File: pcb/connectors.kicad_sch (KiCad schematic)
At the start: 7 parts, among them J1 USB_C_Receptacle_USB2.0, J5 Conn_01x04, U6 USBLC6-2SC6

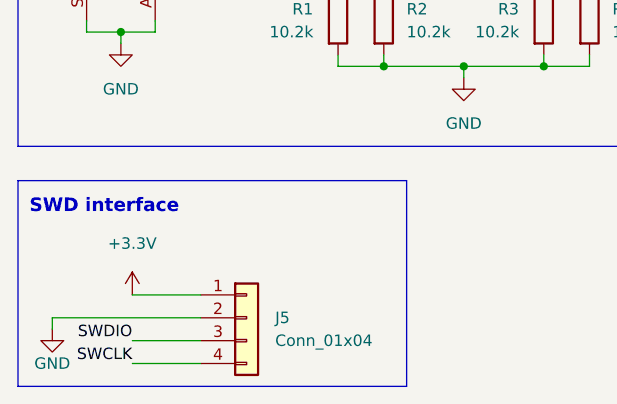
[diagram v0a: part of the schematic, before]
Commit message: Finished off schematic
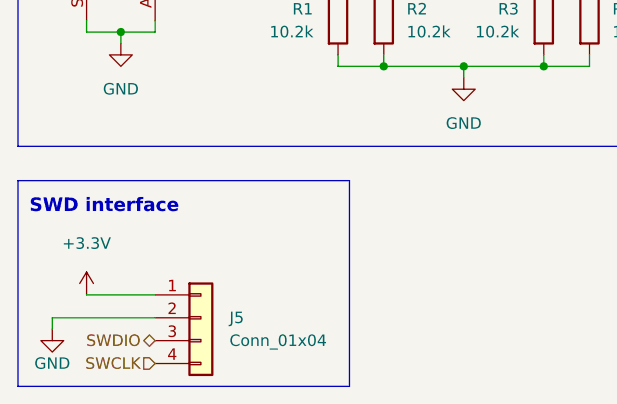
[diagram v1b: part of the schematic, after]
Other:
- moved on the sheet: J5
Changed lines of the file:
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@@
-    (stroke (width 0) (type default))
-  )
-  (wire (pts (xy 38.1 115.57) (xy 45.72 115.57))
     (stroke (width 0) (type default))
   )
@@
     (stroke (width 0) (type default))
   )
-  (wire (pts (xy 38.1 113.03) (xy 45.72 113.03))
-    (stroke (width 0) (type default))
-  )
-  (polyline (pts (xy 68.58 118.11) (xy 25.4 118.11))
+  (polyline (pts (xy 62.23 118.11) (xy 25.4 118.11))
     (stroke (width 0) (type default))
   )
@@
     (stroke (width 0) (type default))
   )
-  (wire (pts (xy 38.1 107.95) (xy 45.72 107.95))
+  (wire (pts (xy 33.02 107.95) (xy 40.64 107.95))
     (stroke (width 0) (type default))
   )
@@
     (stroke (width 0) (type default))
   )
-  (polyline (pts (xy 68.58 95.25) (xy 68.58 118.11))
+  (polyline (pts (xy 62.23 95.25) (xy 62.23 118.11))
     (stroke (width 0) (type default))
   )
@@
     (stroke (width 0) (type default))
   )
-  (wire (pts (xy 29.21 110.49) (xy 45.72 110.49))
+  (wire (pts (xy 29.21 110.49) (xy 40.64 110.49))
     (stroke (width 0) (type default))
   )
@@
     (stroke (width 0) (type default))
   )
-  (polyline (pts (xy 25.4 95.25) (xy 68.58 95.25))
+  (polyline (pts (xy 25.4 95.25) (xy 62.23 95.25))
     (stroke (width 0) (type default))
   )
@@
     (effects (font (size 1.27 1.27)) (justify right bottom))
   )
-  (label "SWDIO" (at 38.1 113.03 180) (fields_autoplaced)
-    (effects (font (size 1.27 1.27)) (justify right bottom))
-  )
-  (label "SWCLK" (at 38.1 115.57 180) (fields_autoplaced)
-    (effects (font (size 1.27 1.27)) (justify right bottom))
-  )
   (hierarchical_label "USB_D+" (shape bidirectional) (at 80.01 66.04 0) (fields_autoplaced)
     (effects (font (size 1.27 1.27)) (justify left))
+  )
+  (hierarchical_label "SWCLK" (shape input) (at 40.64 115.57 180) (fields_autoplaced)
+    (effects (font (size 1.27 1.27)) (justify right))
+  )
+  (hierarchical_label "SWDIO" (shape bidirectional) (at 40.64 113.03 180) (fields_autoplaced)
+    (effects (font (size 1.27 1.27)) (justify right))
   )
   (hierarchical_label "USB_D-" (shape bidirectional) (at 80.01 45.72 0) (fields_autoplaced)
@@
     )
   )
-  (symbol (lib_id "power:+3.3V") (at 38.1 107.95 0) (unit 1)
-    (in_bom yes) (on_board yes) (dnp no) (fields_autoplaced)
-    (property "Reference" "#PWR041" (at 38.1 111.76 0)
-      (effects (font (size 1.27 1.27)) hide)
-    )
-    (property "Value" "+3.3V" (at 38.1 102.235 0)
-      (effects (font (size 1.27 1.27)))
-    )
-    (property "Footprint" "" (at 38.1 107.95 0)
-      (effects (font (size 1.27 1.27)) hide)
-    )
-    (property "Datasheet" "" (at 38.1 107.95 0)
+  (symbol (lib_id "power:+3.3V") (at 33.02 107.95 0) (unit 1)
+    (in_bom yes) (on_board yes) (dnp no) (fields_autoplaced)
+    (property "Reference" "#PWR041" (at 33.02 111.76 0)
+      (effects (font (size 1.27 1.27)) hide)
+    )
+    (property "Value" "+3.3V" (at 33.02 102.235 0)
+      (effects (font (size 1.27 1.27)))
+    )
+    (property "Footprint" "" (at 33.02 107.95 0)
+      (effects (font (size 1.27 1.27)) hide)
+    )
+    (property "Datasheet" "" (at 33.02 107.95 0)
       (effects (font (size 1.27 1.27)) hide)
     )
@@
       (project "keyboard"
         (path "/fc529d87-72d0-4c92-b352-ddcf4c6f7199/953c467c-8c0d-4158-80e9-7f51ef1515ee"
-          (reference "#PWR012") (unit 1)
+          (reference "#PWR011") (unit 1)
         )
       )
@@
     )
   )
-  (symbol (lib_id "Connector_Generic:Conn_01x04") (at 50.8 110.49 0) (unit 1)
-    (in_bom yes) (on_board yes) (dnp no) (fields_autoplaced)
-    (property "Reference" "J5" (at 53.975 110.4899 0)
+  (symbol (lib_id "Connector_Generic:Conn_01x04") (at 45.72 110.49 0) (unit 1)
+    (in_bom yes) (on_board yes) (dnp no) (fields_autoplaced)
+    (property "Reference" "J5" (at 48.895 110.4899 0)
       (effects (font (size 1.27 1.27)) (justify left))
     )
-    (property "Value" "Conn_01x04" (at 53.975 113.0299 0)
+    (property "Value" "Conn_01x04" (at 48.895 113.0299 0)
       (effects (font (size 1.27 1.27)) (justify left))
     )
-    (property "Footprint" "Connector_PinHeader_2.54mm:PinHeader_1x04_P2.54mm_Vertical" (at 50.8 110.49 0)
-      (effects (font (size 1.27 1.27)) hide)
-    )
-    (property "Datasheet" "~" (at 50.8 110.49 0)
+    (property "Footprint" "Connector_PinHeader_2.54mm:PinHeader_1x04_P2.54mm_Vertical" (at 45.72 110.49 0)
+      (effects (font (size 1.27 1.27)) hide)
+    )
+    (property "Datasheet" "~" (at 45.72 110.49 0)
       (effects (font (size 1.27 1.27)) hide)
     )
@@
   (symbol (lib_id "power:GND") (at 36.83 80.01 0) (unit 1)
     (in_bom yes) (on_board yes) (dnp no) (fields_autoplaced)
-    (property "Reference" "#PWR011" (at 36.83 86.36 0)
+    (property "Reference" "#PWR012" (at 36.83 86.36 0)
       (effects (font (size 1.27 1.27)) hide)
     )
@@
       (project "keyboard"
         (path "/fc529d87-72d0-4c92-b352-ddcf4c6f7199/953c467c-8c0d-4158-80e9-7f51ef1515ee"
-          (reference "#PWR011") (unit 1)
-        )
-      )
+          (reference "#PWR012") (unit 1)
+        )
+      )

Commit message: Started routing
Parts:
- J5: footprint Connector_PinHeader_2.54mm:PinHeader_1x04_P2.54mm_Vertical -> Connector_PinSocket_2.54mm:PinSocket_1x04_P2.54mm_Vertical
- R1, R2, R3, R4: footprint Resistor_SMD:R_0201_0603Metric -> Resistor_SMD:R_0603_1608Metric
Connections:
- net VBUS: now reaches J1.A4 (VBUS), J1.A9 (VBUS), J1.B4 (VBUS), J1.B9 (VBUS), U6.5 (VBUS)
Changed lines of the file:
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@@
   (junction (at 57.15 53.34) (diameter 0) (color 0 0 0 0)
+  )
+  (junction (at 73.66 39.37) (diameter 0) (color 0 0 0 0)
   )
   (junction (at 86.36 72.39) (diameter 0) (color 0 0 0 0)
@@
     (stroke (width 0) (type default))
   )
+  (wire (pts (xy 73.66 39.37) (xy 90.17 39.37))
+    (stroke (width 0) (type default))
+  )
   (wire (pts (xy 78.74 45.72) (xy 80.01 45.72))
     (stroke (width 0) (type default))
@@
     (stroke (width 0) (type default))
   )
+  (wire (pts (xy 73.66 38.1) (xy 73.66 39.37))
+    (stroke (width 0) (type default))
+  )
   (wire (pts (xy 90.17 55.88) (xy 86.36 55.88))
     (stroke (width 0) (type default))
   )
-  (wire (pts (xy 55.88 39.37) (xy 90.17 39.37))
+  (wire (pts (xy 55.88 39.37) (xy 73.66 39.37))
     (stroke (width 0) (type default))
   )
@@
         (path "/fc529d87-72d0-4c92-b352-ddcf4c6f7199/953c467c-8c0d-4158-80e9-7f51ef1515ee"
           (reference "U2") (unit 1)
+        )
+      )
+    )
+  )
+  (symbol (lib_id "Device:R") (at 88.9 77.47 0) (unit 1)
+    (in_bom yes) (on_board yes) (dnp no)
+    (property "Reference" "R4" (at 91.44 76.2 0)
+      (effects (font (size 1.27 1.27)) (justify left))
+    )
+    (property "Value" "10.2k" (at 91.44 78.74 0)
+      (effects (font (size 1.27 1.27)) (justify left))
+    )
+    (property "Footprint" "Resistor_SMD:R_0603_1608Metric" (at 87.122 77.47 90)
+      (effects (font (size 1.27 1.27)) hide)
+    )
+    (property "Datasheet" "~" (at 88.9 77.47 0)
+      (effects (font (size 1.27 1.27)) hide)
+    )
+    (pin "1")
+    (pin "2")
+    (instances
+      (project "keyboard"
+        (path "/fc529d87-72d0-4c92-b352-ddcf4c6f7199/953c467c-8c0d-4158-80e9-7f51ef1515ee"
+          (reference "R4") (unit 1)
         )
       )
@@
       (effects (font (size 1.27 1.27)) (justify left))
     )
-    (property "Footprint" "Connector_PinHeader_2.54mm:PinHeader_1x04_P2.54mm_Vertical" (at 45.72 110.49 0)
+    (property "Footprint" "Connector_PinSocket_2.54mm:PinSocket_1x04_P2.54mm_Vertical" (at 45.72 110.49 0)
       (effects (font (size 1.27 1.27)) hide)
     )
@@
     )
   )
+  (symbol (lib_id "power:VBUS") (at 73.66 38.1 0) (unit 1)
+    (in_bom yes) (on_board yes) (dnp no) (fields_autoplaced)
+    (property "Reference" "#PWR034" (at 73.66 41.91 0)
+      (effects (font (size 1.27 1.27)) hide)
+    )
+    (property "Value" "VBUS" (at 73.66 34.29 0)
+      (effects (font (size 1.27 1.27)))
+    )
+    (property "Footprint" "" (at 73.66 38.1 0)
+      (effects (font (size 1.27 1.27)) hide)
+    )
+    (property "Datasheet" "" (at 73.66 38.1 0)
+      (effects (font (size 1.27 1.27)) hide)
+    )
+    (pin "1")
+    (instances
+      (project "keyboard"
+        (path "/fc529d87-72d0-4c92-b352-ddcf4c6f7199/953c467c-8c0d-4158-80e9-7f51ef1515ee"
+          (reference "#PWR034") (unit 1)
+        )
+      )
+    )
+  )
   (symbol (lib_id "Device:R") (at 83.82 77.47 0) (unit 1)
     (in_bom yes) (on_board yes) (dnp no)
@@
       (effects (font (size 1.27 1.27)) (justify left))
     )
-    (property "Footprint" "Resistor_SMD:R_0201_0603Metric" (at 82.042 77.47 90)
+    (property "Footprint" "Resistor_SMD:R_0603_1608Metric" (at 82.042 77.47 90)
       (effects (font (size 1.27 1.27)) hide)
     )
@@
         (path "/fc529d87-72d0-4c92-b352-ddcf4c6f7199/953c467c-8c0d-4158-80e9-7f51ef1515ee"
           (reference "R3") (unit 1)
-        )
-      )
-    )
-  )
-  (symbol (lib_id "Device:R") (at 88.9 77.47 0) (unit 1)
-    (in_bom yes) (on_board yes) (dnp no)
-    (property "Reference" "R4" (at 91.44 76.2 0)
-      (effects (font (size 1.27 1.27)) (justify left))
-    )
-    (property "Value" "10.2k" (at 91.44 78.74 0)
-      (effects (font (size 1.27 1.27)) (justify left))
-    )
-    (property "Footprint" "Resistor_SMD:R_0201_0603Metric" (at 87.122 77.47 90)
-      (effects (font (size 1.27 1.27)) hide)
-    )
-    (property "Datasheet" "~" (at 88.9 77.47 0)
-      (effects (font (size 1.27 1.27)) hide)
-    )
-    (pin "1")
-    (pin "2")
-    (instances
-      (project "keyboard"
-        (path "/fc529d87-72d0-4c92-b352-ddcf4c6f7199/953c467c-8c0d-4158-80e9-7f51ef1515ee"
-          (reference "R4") (unit 1)
         )
       )
@@
       (effects (font (size 1.27 1.27)) (justify left))
     )
-    (property "Footprint" "Resistor_SMD:R_0201_0603Metric" (at 59.182 77.47 90)
+    (property "Footprint" "Resistor_SMD:R_0603_1608Metric" (at 59.182 77.47 90)
       (effects (font (size 1.27 1.27)) hide)
     )
@@
       (effects (font (size 1.27 1.27)) (justify left))
     )
-    (property "Footprint" "Resistor_SMD:R_0201_0603Metric" (at 64.262 77.47 90)
-      (effects (font (size 1.27 1.27)) hide)
-    )
+    (property "Footprint" "Resistor_SMD:R_0603_1608Metric" (at 64.262 77.47 90)
+      (effects (font (size 1.27 1.27)) hide)
+    )

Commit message: Finished routing, ready for checks
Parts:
- J5: footprint Connector_PinSocket_2.54mm:PinSocket_1x04_P2.54mm_Vertical -> Connector_PinSocket_2.54mm:PinSocket_1x04_P2.54mm_Horizontal
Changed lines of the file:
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@@
       (effects (font (size 1.27 1.27)) (justify left))
     )
-    (property "Footprint" "Connector_PinSocket_2.54mm:PinSocket_1x04_P2.54mm_Vertical" (at 45.72 110.49 0)
+    (property "Footprint" "Connector_PinSocket_2.54mm:PinSocket_1x04_P2.54mm_Horizontal" (at 45.72 110.49 0)
       (effects (font (size 1.27 1.27)) hide)
     )

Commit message: Creating production files
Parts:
- J5: LCSC (none) -> C2897386
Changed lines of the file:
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@@
+      (effects (font (size 1.27 1.27)) hide)
+    )
+    (property "LCSC" "C2897386" (at 45.72 110.49 0)
       (effects (font (size 1.27 1.27)) hide)
     )
